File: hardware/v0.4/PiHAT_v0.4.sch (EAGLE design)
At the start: 40 parts, among them IC1 BMP280, J1 FTDI, J3 ISP, U1 ATMEGA328P, U10 TSL2591, U3 OPA344, U6 ADMP401, U8 CCS811, Y1 16MHZ

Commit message: Adjusted silkscreen
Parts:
- U2: value (none) -> SHT31
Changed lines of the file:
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@@
 <?xml version="1.0" encoding="utf-8"?>
 <!DOCTYPE eagle SYSTEM "eagle.dtd">
-<eagle version="7.7.0">
+<eagle version="8.0.2">
 <drawing>
 <settings>
@@
 <part name="GND6" library="SparkFun-Aesthetics" deviceset="GND" device=""/>
 <part name="SUPPLY14" library="SparkFun-Aesthetics" deviceset="VCC" device=""/>
-<part name="U2" library="Adafruit SHT31" deviceset="SHT3X" device="">
+<part name="U2" library="Adafruit SHT31" deviceset="SHT3X" device="" value="SHT31">
 <attribute name="MPN" value="SHT35-DIS-B"/>
 </part>

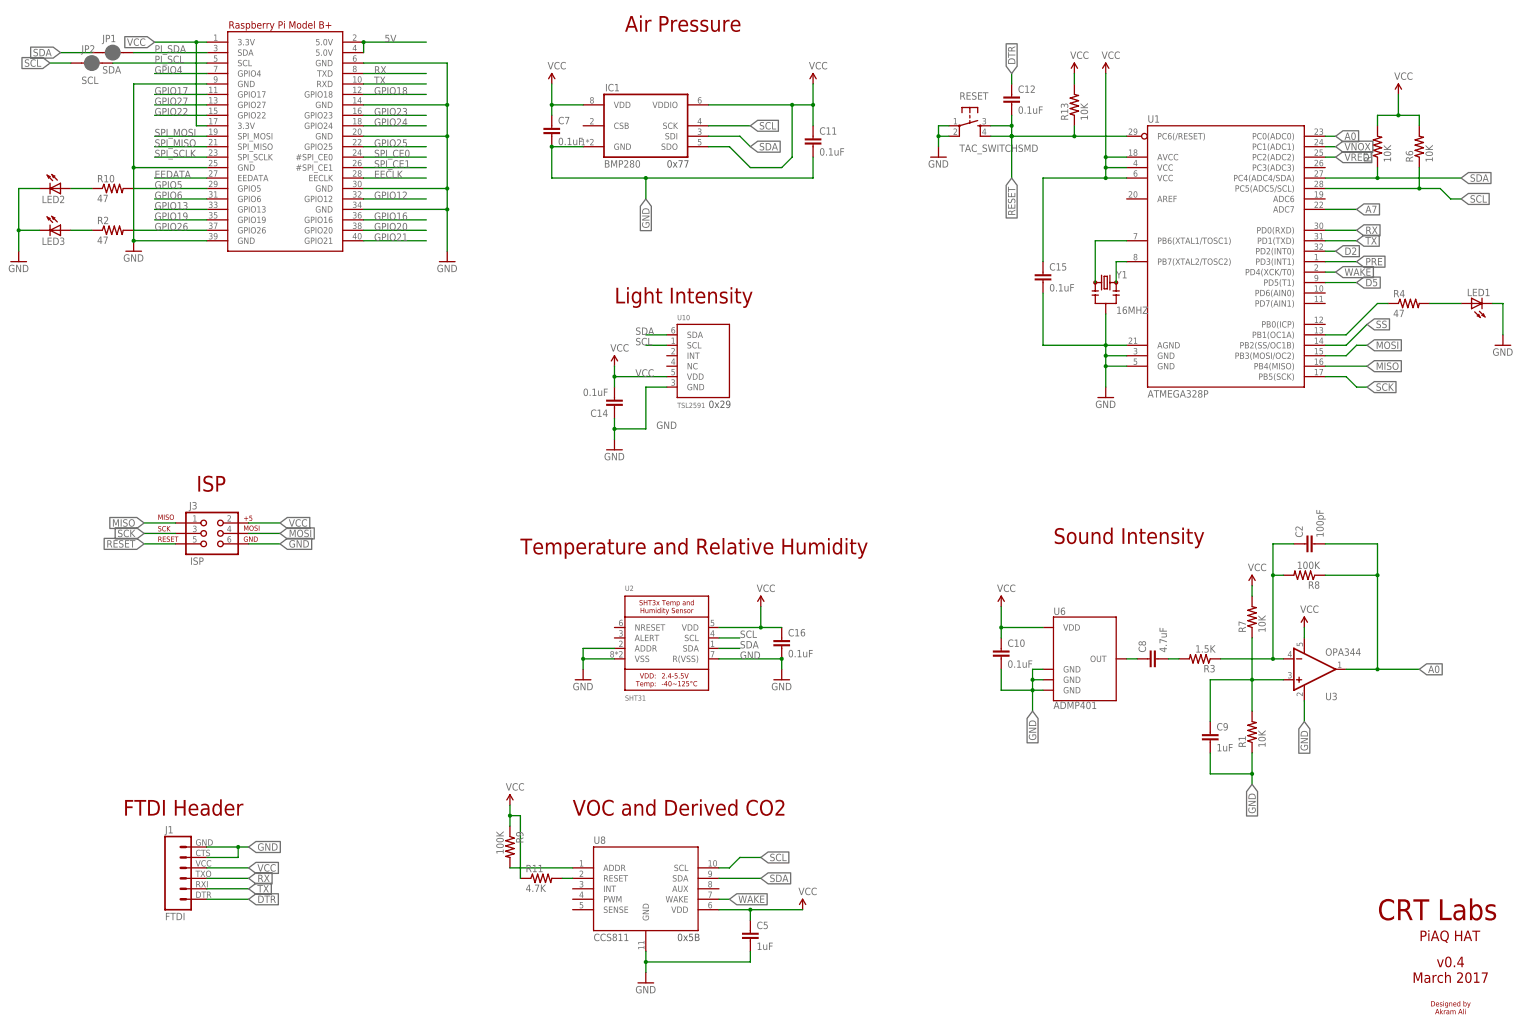
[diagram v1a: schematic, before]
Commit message: Added RGB LED
- RGB LED on pin 6
- Rearragned other LED on pin 9 and adjusted trace
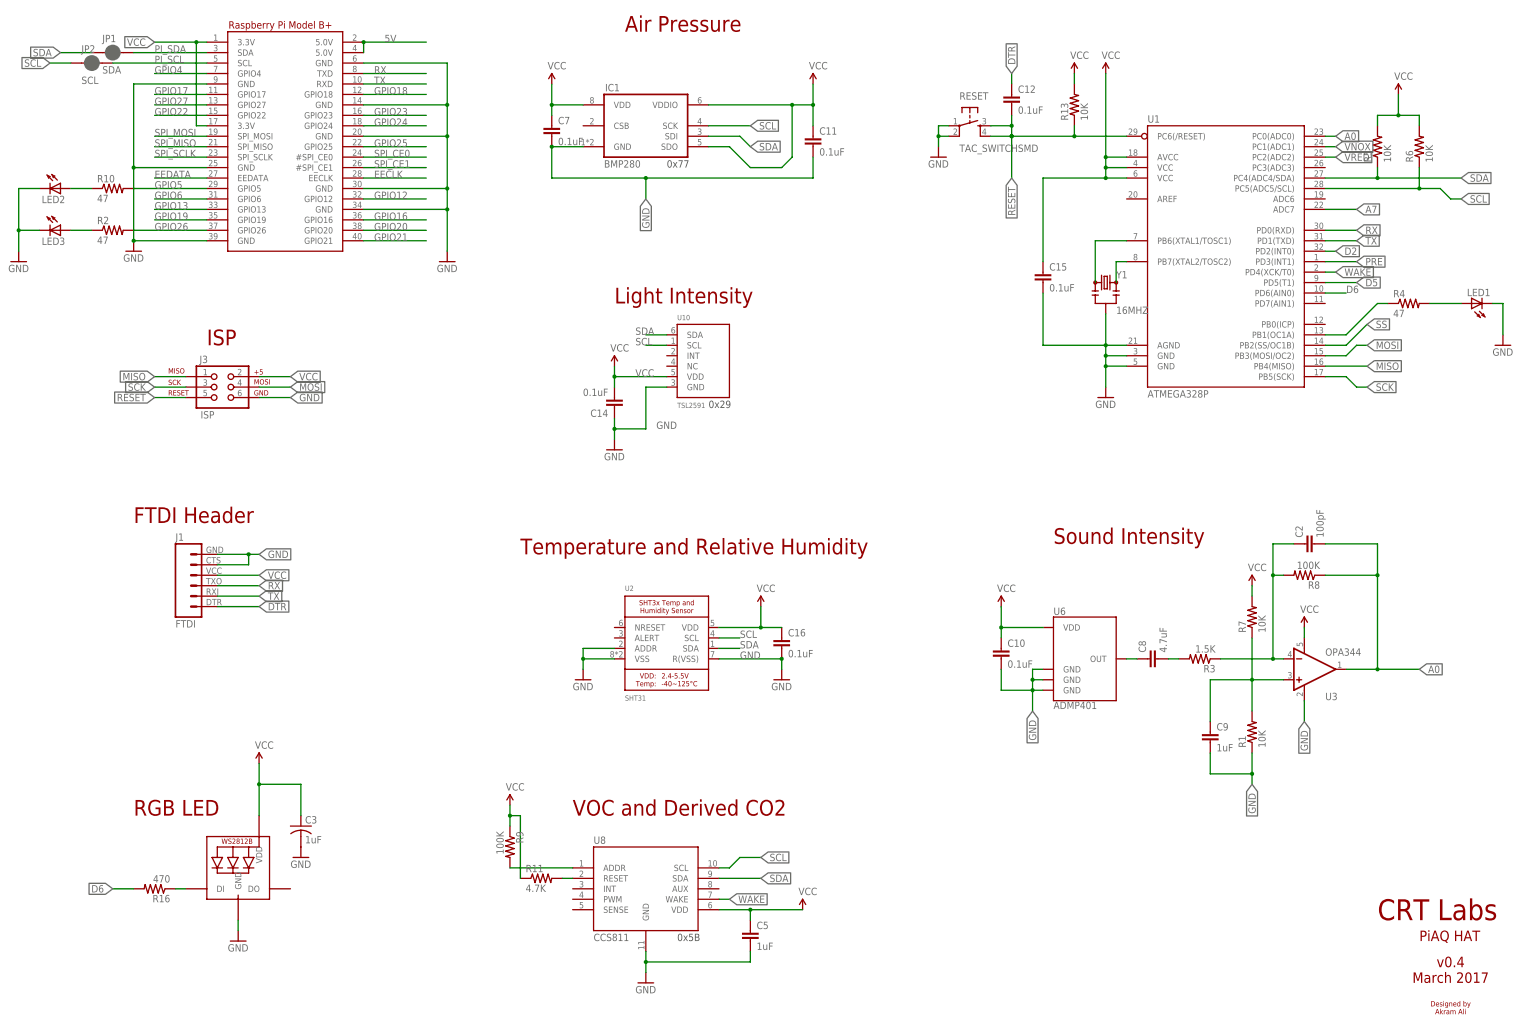
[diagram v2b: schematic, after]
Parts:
- added C3: 1uF, adafruit:C-USC0603K
- added R16: 470, adafruit:R-US_R0603
- added RGBLED: WS2812B3535, adafruit:WS2812B3535
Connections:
- new net D6: R16.2, U1.PD6(AIN0)
- new net N$12: R16.1, RGBLED.DI
- net GND: now also C3.2, RGBLED.GND
- net VCC: now also C3.1, RGBLED.VDD
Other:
- note added: "RGB LED"
- moved on the sheet: J1, J3
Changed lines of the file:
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@@
 <attribute name="MPN" value="RC0805FR-07100KL"/>
+</part>
+<part name="R16" library="adafruit" deviceset="R-US_" device="R0603" value="470">
+<attribute name="MPN" value="RC0805FR-07470RL "/>
+</part>
+<part name="GND11" library="supply1" deviceset="GND" device=""/>
+<part name="C3" library="adafruit" deviceset="C-US" device="C0603K" value="1uF">
+<attribute name="MPN" value="CC0805ZRY5V8BB105"/>
+</part>
+<part name="GND12" library="supply1" deviceset="GND" device=""/>
+<part name="SUPPLY15" library="SparkFun-Aesthetics" deviceset="VCC" device=""/>
+<part name="RGBLED" library="adafruit" deviceset="WS2812B" device="3535">
+<attribute name="MPN" value="SK6812 mini"/>
 </part>
 </parts>
@@
 <text x="411.48" y="2.54" size="3.81" layer="94">Sound Intensity</text>
 <text x="281.94" y="0" size="3.81" layer="94">Temperature and Relative Humidity</text>
-<text x="203.2" y="15.24" size="3.81" layer="94">ISP</text>
+<text x="205.74" y="50.8" size="3.81" layer="94">ISP</text>
 <text x="490.22" y="-88.9" size="5.08" layer="94" font="vector" ratio="20">CRT Labs</text>
 <text x="500.38" y="-93.98" size="2.54" layer="94" font="vector" ratio="10">PiAQ HAT</text>
@@
 Akram Ali</text>
 <text x="320.04" y="-93.98" size="1.778" layer="97">0x5B</text>
-<text x="185.42" y="-63.5" size="3.81" layer="94">FTDI Header</text>
+<text x="187.96" y="7.62" size="3.81" layer="94">FTDI Header</text>
 <text x="317.5" y="93.98" size="1.778" layer="97">0x77</text>
 <frame x1="137.16" y1="-127" x2="541.02" y2="154.94" columns="8" rows="5" layer="94"/>
 <text x="304.8" y="60.96" size="3.81" layer="94">Light Intensity</text>
 <text x="327.66" y="35.56" size="1.778" layer="97">0x29</text>
+<text x="187.96" y="-63.5" size="3.81" layer="94">RGB LED</text>
 </plain>
 <instances>
@@
 <attribute name="MPN" x="170.18" y="88.9" size="1.778" layer="96" rot="R90" display="off"/>
 </instance>
-<instance part="J1" gate="G$1" x="200.66" y="-78.74">
-<attribute name="NO_BOM" x="200.66" y="-78.74" size="1.778" layer="96" display="off"/>
-</instance>
-<instance part="J3" gate="G$1" x="205.74" y="5.08">
-<attribute name="NO_BOM" x="205.74" y="5.08" size="1.778" layer="96" display="off"/>
+<instance part="J1" gate="G$1" x="203.2" y="-7.62">
+<attribute name="NO_BOM" x="203.2" y="-7.62" size="1.778" layer="96" display="off"/>
+</instance>
+<instance part="J3" gate="G$1" x="208.28" y="40.64">
+<attribute name="NO_BOM" x="208.28" y="40.64" size="1.778" layer="96" display="off"/>
 </instance>
 <instance part="IC1" gate="G$1" x="312.42" y="104.14">
@@
 <instance part="R11" gate="G$1" x="287.02" y="-78.74">
 <attribute name="MPN" x="287.02" y="-78.74" size="1.778" layer="96" display="off"/>
+</instance>
+<instance part="R16" gate="G$1" x="193.04" y="-81.28" rot="R180">
+<attribute name="MPN" x="193.04" y="-81.28" size="1.778" layer="96" rot="R180" display="off"/>
+</instance>
+<instance part="GND11" gate="1" x="213.36" y="-93.98"/>
+<instance part="C3" gate="G$1" x="228.6" y="-66.04">
+<attribute name="MPN" x="228.6" y="-66.04" size="1.778" layer="96" display="off"/>
+</instance>
+<instance part="GND12" gate="1" x="228.6" y="-73.66"/>
+<instance part="SUPPLY15" gate="G$1" x="218.44" y="-50.8"/>
+<instance part="RGBLED" gate="G$1" x="213.36" y="-78.74">
+<attribute name="MPN" x="213.36" y="-78.74" size="1.778" layer="96" display="off"/>
 </instance>
 </instances>
@@
 <segment>
 <pinref part="J3" gate="G$1" pin="6"/>
-<wire x1="215.9" y1="2.54" x2="223.52" y2="2.54" width="0.1524" layer="91"/>
-<label x="223.52" y="2.54" size="1.778" layer="95" xref="yes"/>
+<wire x1="218.44" y1="38.1" x2="226.06" y2="38.1" width="0.1524" layer="91"/>
+<label x="226.06" y="38.1" size="1.778" layer="95" xref="yes"/>
 </segment>
 <segment>
 <pinref part="J1" gate="G$1" pin="5"/>
-<wire x1="205.74" y1="-73.66" x2="213.36" y2="-73.66" width="0.1524" layer="91"/>
+<wire x1="208.28" y1="-2.54" x2="215.9" y2="-2.54" width="0.1524" layer="91"/>
 <pinref part="J1" gate="G$1" pin="6"/>
-<wire x1="205.74" y1="-71.12" x2="213.36" y2="-71.12" width="0.1524" layer="91"/>
-<wire x1="213.36" y1="-71.12" x2="215.9" y2="-71.12" width="0.1524" layer="91"/>
-<wire x1="213.36" y1="-73.66" x2="213.36" y2="-71.12" width="0.1524" layer="91"/>
-<junction x="213.36" y="-71.12"/>
-<label x="215.9" y="-71.12" size="1.778" layer="95" xref="yes"/>
+<wire x1="208.28" y1="0" x2="215.9" y2="0" width="0.1524" layer="91"/>
+<wire x1="215.9" y1="0" x2="218.44" y2="0" width="0.1524" layer="91"/>
+<wire x1="215.9" y1="-2.54" x2="215.9" y2="0" width="0.1524" layer="91"/>
+<junction x="215.9" y="0"/>
+<label x="218.44" y="0" size="1.778" layer="95" xref="yes"/>
 </segment>
 <segment>
@@
 <wire x1="297.18" y1="-22.86" x2="297.18" y2="-25.4" width="0.1524" layer="91"/>
 <junction x="297.18" y="-25.4"/>
+</segment>
+<segment>
+<pinref part="GND11" gate="1" pin="GND"/>
+<wire x1="213.36" y1="-91.44" x2="213.36" y2="-88.9" width="0.1524" layer="91"/>
+<pinref part="RGBLED" gate="G$1" pin="GND"/>
+</segment>
+<segment>
+<pinref part="C3" gate="G$1" pin="2"/>
+<pinref part="GND12" gate="1" pin="GND"/>
 </segment>
 </net>
@@
 <segment>
 <pinref part="J3" gate="G$1" pin="2"/>
-<wire x1="215.9" y1="7.62" x2="223.52" y2="7.62" width="0.1524" layer="91"/>
-<label x="223.52" y="7.62" size="1.778" layer="95" xref="yes"/>
+<wire x1="218.44" y1="43.18" x2="226.06" y2="43.18" width="0.1524" layer="91"/>
+<label x="226.06" y="43.18" size="1.778" layer="95" xref="yes"/>
 </segment>
 <segment>
 <pinref part="J1" gate="G$1" pin="4"/>
-<wire x1="205.74" y1="-76.2" x2="215.9" y2="-76.2" width="0.1524" layer="91"/>
-<label x="215.9" y="-76.2" size="1.778" layer="95" xref="yes"/>
+<wire x1="208.28" y1="-5.08" x2="218.44" y2="-5.08" width="0.1524" layer="91"/>
+<label x="218.44" y="-5.08" size="1.778" layer="95" xref="yes"/>
 </segment>
 <segment>
@@
 <junction x="340.36" y="-17.78"/>
 </segment>
+<segment>
+<pinref part="SUPPLY15" gate="G$1" pin="VCC"/>
+<pinref part="RGBLED" gate="G$1" pin="VDD"/>
+<wire x1="218.44" y1="-63.5" x2="218.44" y2="-55.88" width="0.1524" layer="91"/>
+<pinref part="C3" gate="G$1" pin="1"/>
+<wire x1="218.44" y1="-55.88" x2="218.44" y2="-50.8" width="0.1524" layer="91"/>
+<wire x1="228.6" y1="-63.5" x2="228.6" y2="-55.88" width="0.1524" layer="91"/>
+<wire x1="228.6" y1="-55.88" x2="218.44" y2="-55.88" width="0.1524" layer="91"/>
+<junction x="218.44" y="-55.88"/>
+</segment>
 </net>
 <net name="D5" class="0">
@@
 <segment>
 <pinref part="J3" gate="G$1" pin="1"/>
-<wire x1="198.12" y1="7.62" x2="190.5" y2="7.62" width="0.1524" layer="91"/>
-<label x="190.5" y="7.62" size="1.778" layer="95" rot="R180" xref="yes"/>
+<wire x1="200.66" y1="43.18" x2="193.04" y2="43.18" width="0.1524" layer="91"/>
+<label x="193.04" y="43.18" size="1.778" layer="95" rot="R180" xref="yes"/>
 </segment>
 </net>
@@
 <segment>
 <pinref part="J3" gate="G$1" pin="3"/>
-<wire x1="198.12" y1="5.08" x2="190.5" y2="5.08" width="0.1524" layer="91"/>
-<label x="190.5" y="5.08" size="1.778" layer="95" rot="R180" xref="yes"/>
+<wire x1="200.66" y1="40.64" x2="193.04" y2="40.64" width="0.1524" layer="91"/>
+<label x="193.04" y="40.64" size="1.778" layer="95" rot="R180" xref="yes"/>
 </segment>
 </net>
@@
 <segment>
 <pinref part="J3" gate="G$1" pin="5"/>
-<wire x1="198.12" y1="2.54" x2="190.5" y2="2.54" width="0.1524" layer="91"/>
-<label x="190.5" y="2.54" size="1.778" layer="95" rot="R180" xref="yes"/>
+<wire x1="200.66" y1="38.1" x2="193.04" y2="38.1" width="0.1524" layer="91"/>
+<label x="193.04" y="38.1" size="1.778" layer="95" rot="R180" xref="yes"/>
 </segment>
 </net>
@@
 <segment>
 <pinref part="J3" gate="G$1" pin="4"/>
-<wire x1="215.9" y1="5.08" x2="223.52" y2="5.08" width="0.1524" layer="91"/>
-<label x="223.52" y="5.08" size="1.778" layer="95" xref="yes"/>
+<wire x1="218.44" y1="40.64" x2="226.06" y2="40.64" width="0.1524" layer="91"/>
+<label x="226.06" y="40.64" size="1.778" layer="95" xref="yes"/>
 </segment>
 </net>
@@
 <segment>
 <pinref part="J1" gate="G$1" pin="1"/>
-<wire x1="205.74" y1="-83.82" x2="215.9" y2="-83.82" width="0.1524" layer="91"/>
-<label x="215.9" y="-83.82" size="1.778" layer="95" xref="yes"/>
+<wire x1="208.28" y1="-12.7" x2="218.44" y2="-12.7" width="0.1524" layer="91"/>
+<label x="218.44" y="-12.7" size="1.778" layer="95" xref="yes"/>
 </segment>
 </net>
@@
 <segment>
 <pinref part="J1" gate="G$1" pin="3"/>
-<wire x1="205.74" y1="-78.74" x2="215.9" y2="-78.74" width="0.1524" layer="91"/>
-<label x="215.9" y="-78.74" size="1.778" layer="95" xref="yes"/>
+<wire x1="208.28" y1="-7.62" x2="218.44" y2="-7.62" width="0.1524" layer="91"/>
+<label x="218.44" y="-7.62" size="1.778" layer="95" xref="yes"/>
 </segment>
 </net>
@@
 <segment>
 <pinref part="J1" gate="G$1" pin="2"/>
-<wire x1="205.74" y1="-81.28" x2="215.9" y2="-81.28" width="0.1524" layer="91"/>
-<label x="215.9" y="-81.28" size="1.778" layer="95" xref="yes"/>
+<wire x1="208.28" y1="-10.16" x2="218.44" y2="-10.16" width="0.1524" layer="91"/>
+<label x="218.44" y="-10.16" size="1.778" layer="95" xref="yes"/>
 </segment>
 </net>
@@
 </segment>
 </net>
+<net name="N$12" class="0">
+<segment>
+<pinref part="R16" gate="G$1" pin="1"/>
+<wire x1="198.12" y1="-81.28" x2="200.66" y2="-81.28" width="0.1524" layer="91"/>
+<pinref part="RGBLED" gate="G$1" pin="DI"/>
+</segment>
+</net>
+<net name="D6" class="0">
+<segment>
+<pinref part="R16" gate="G$1" pin="2"/>
+<wire x1="182.88" y1="-81.28" x2="187.96" y2="-81.28" width="0.1524" layer="91"/>
+<label x="182.88" y="-81.28" size="1.778" layer="95" rot="R180" xref="yes"/>
+</segment>
+<segment>
+<pinref part="U1" gate="U$1" pin="PD6(AIN0)"/>
+<wire x1="477.52" y1="63.5" x2="482.6" y2="63.5" width="0.1524" layer="91"/>
+<label x="482.6" y="63.5" size="1.778" layer="95"/>
+</segment>
+</net>
